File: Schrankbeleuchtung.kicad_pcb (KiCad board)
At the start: 2 copper layers, 77 x 60 mm, 27 parts, among them J1 Jack-DC, J2 Conn_01x02, J3 Conn_01x02, J4 Conn_01x02, J5 Conn_01x02, J6 Conn_01x02, J7 Conn_01x02, J8 Conn_01x02, J9 Conn_01x02, Q1 AO3400A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

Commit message: Edit description
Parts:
- moved J6 92.6 mm to (56.8, 71.0)
- moved J7 92.2 mm to (66.2, 71.0)
- moved J9 92.0 mm to (85.8, 71.0)
- moved J8 91.8 mm to (76.2, 71.0)
- moved Q4 75.6 mm to (63.4, 55.5), turned to 180 degrees
- moved Q3 75.0 mm to (59.5, 55.5), turned to 180 degrees
- moved Q2 74.2 mm to (55.5, 55.5), turned to 180 degrees
- moved Q1 73.5 mm to (51.6, 55.5), turned to 180 degrees
- moved R1 68.1 mm to (53.0, 60.5), turned to 90 degrees
- moved R2 68.1 mm to (56.5, 60.5), turned to 90 degrees
- moved R3 68.1 mm to (60.0, 60.5), turned to 90 degrees
- moved R4 68.1 mm to (63.5, 60.5), turned to 90 degrees
- moved R5 68.1 mm to (67.0, 60.5), turned to 90 degrees
- moved R6 68.1 mm to (70.5, 60.5), turned to 90 degrees
- moved R7 68.1 mm to (74.0, 60.5), turned to 90 degrees
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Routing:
- net +12V: track 29.7 -> 147.1 mm
- net +3.3V: track 75.3 -> 32.8 mm
- net Net-(J4-Pin_2): track 14.1 -> 50.4 mm
- net /GPIO09: track 54.2 -> 21.0 mm
- net /GPIO08: track 46.2 -> 13.4 mm
- net Net-(J5-Pin_2): track 19.3 -> 50.4 mm
- net Net-(J3-Pin_2): track 9.89 -> 40.0 mm
- net /GPIO07: track 41.1 -> 11.6 mm
- net Net-(J2-Pin_2): track 5.98 -> 30.0 mm
- net /GPIO06: track 34.5 -> 19.5 mm
- net /GPIO02: track 0.00 -> 4.05 mm
- net /GPIO05: track 5.90 -> 3.61 mm
- net /GPIO04: track 4.92 -> 3.21 mm
- net /GPIO03: track 4.65 -> 3.36 mm
- net GND: track 15.9 -> 14.8 mm
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- added copper zone on B.Cu, net GND
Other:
- board size 77 x 60 mm -> 55 x 60 mm

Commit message: Edit PCB layout
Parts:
- added H1: MountingHole_Pad, MountingHole:MountingHole_2.2mm_M2_ISO7380_Pad, F.Cu at (49.0, 83.0)
- added H2: MountingHole_Pad, MountingHole:MountingHole_2.2mm_M2_ISO7380_Pad, F.Cu at (96.0, 83.0)
- added H3: MountingHole_Pad, MountingHole:MountingHole_2.2mm_M2_ISO7380_Pad, F.Cu at (96.0, 31.0)
- A1: value RaspberryPi_Pico -> SC0918
- C1: value 220µF -> 100µF; footprint Capacitor_SMD:C_1206_3216Metric -> Capacitor_SMD:CP_Elec_6.3x5.8
- C2: value 220µF -> 100µF; footprint Capacitor_SMD:C_1206_3216Metric -> Capacitor_SMD:C_1210_3225Metric
- J1: value Jack-DC -> 694106301002; footprint Connector_BarrelJack:BarrelJack_GCT_DCJ200-10-A_Horizontal -> Connector_BarrelJack:BarrelJack_Horizontal
- J2, J3, J4, J5, J6, J7, J8, J9: value Conn_01x02 -> B2B-XH-AMLFSNP
- L1: value DR127-330-R -> 33µH; footprint footprints:IND_DR127-330-R_EAT -> Inductor_SMD:L_7.3x7.3_H3.5
- Q1, Q2, Q3, Q4: value AO3400A -> IRLML6344
- moved D1 4.27 mm to (93.5, 40.0), turned to 0 degrees
- moved C2 3.61 mm to (81.0, 31.0), turned to 90 degrees
- moved L1 3.35 mm to (89.0, 32.5), turned to 180 degrees
- moved C1 3.00 mm to (81.0, 38.5)
- moved U1 1.22 mm to (65.3, 35.0)
- moved J1 1.20 mm to (55.5, 35.0), turned to 0 degrees
- moved Q3 0.08 mm to (59.4, 55.5)
- moved Q4 0.06 mm to (63.5, 55.5)
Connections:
- J1 pad 3: (no net) -> unconnected-(J1-Pad3)
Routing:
- net GND: track 14.8 -> 109.8 mm, vias 10 -> 26
- net +12V: track 147.1 -> 142.4 mm
- net Net-(U1-FB): track 18.4 -> 14.9 mm
- net +5V: track 52.1 -> 54.2 mm
- net (no net): vias 3 -> 0

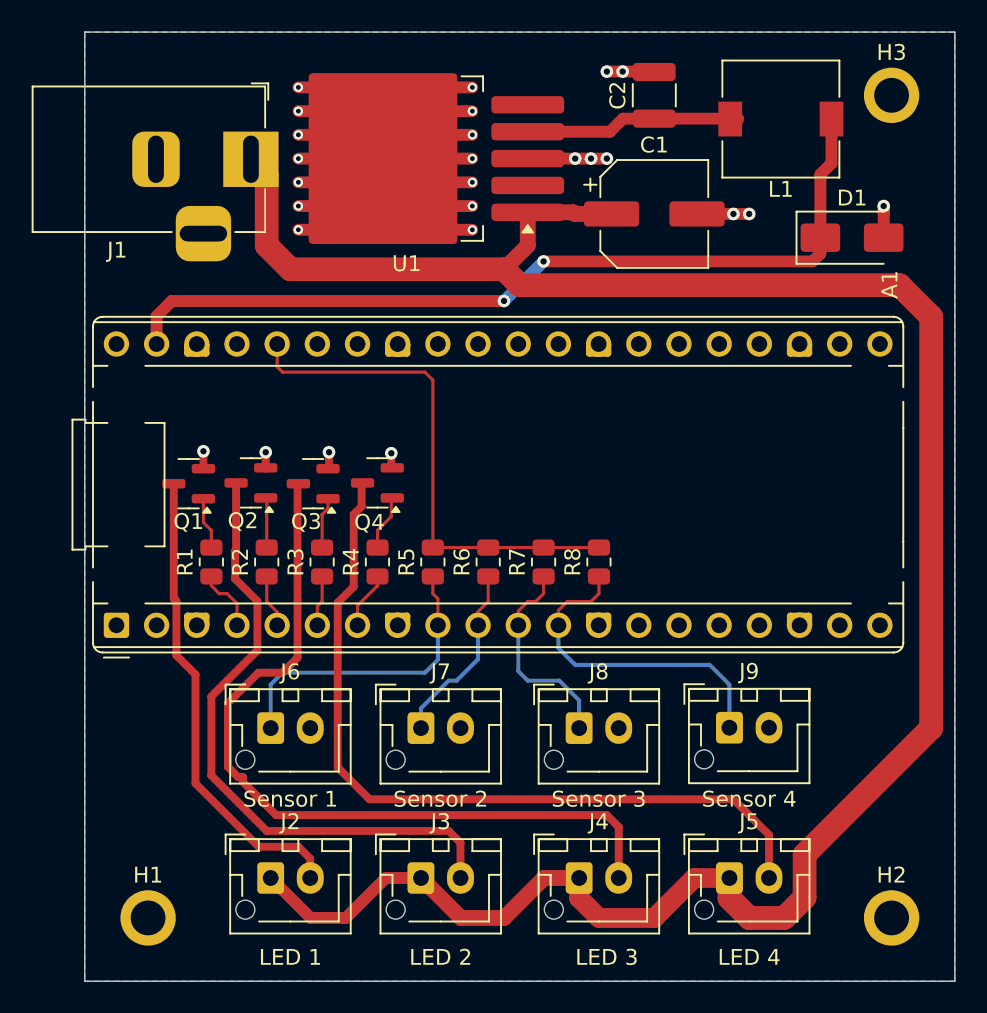
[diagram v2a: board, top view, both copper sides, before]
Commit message: Spannungswandler geändert. Stückliste aktualisiert.
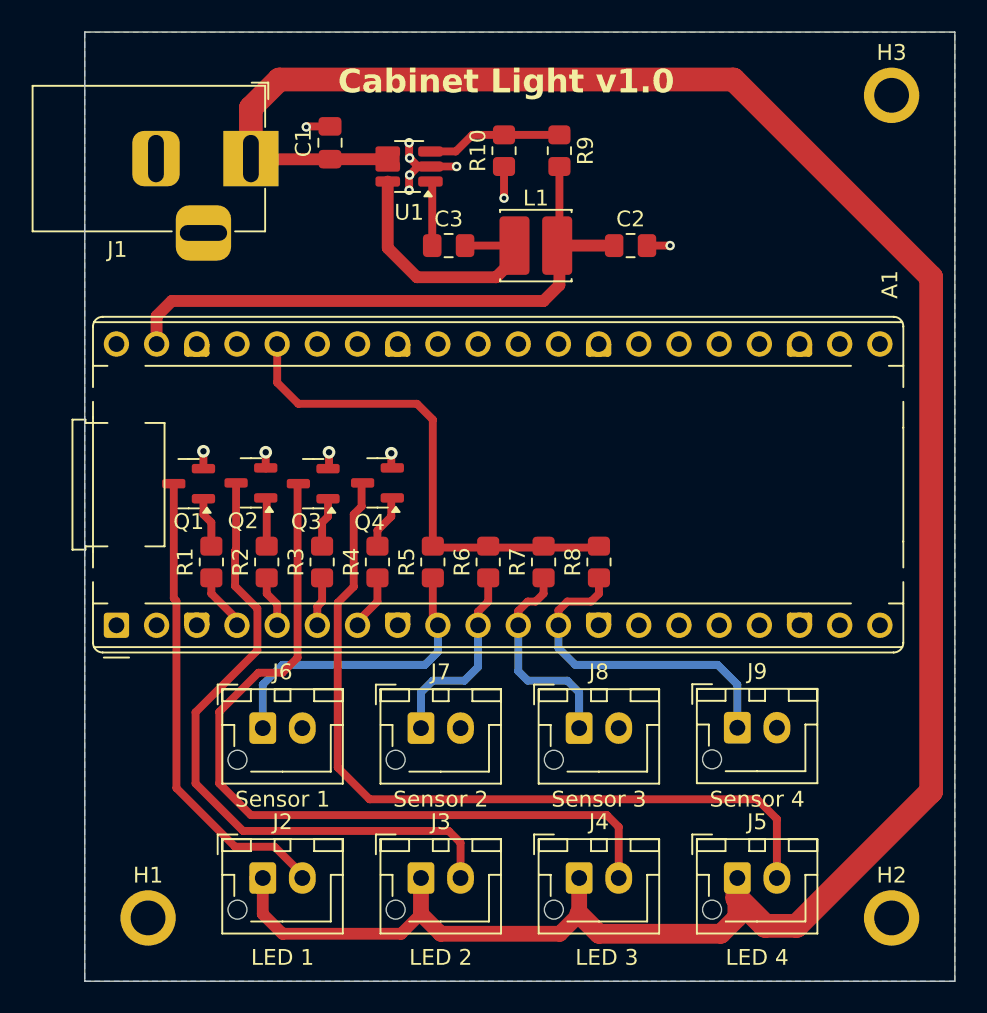
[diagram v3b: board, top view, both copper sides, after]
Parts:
- removed D1: SS34, Diode_SMD:D_SMA
- added C3: 0.1µF, Capacitor_SMD:C_0805_2012Metric_Pad1.18x1.45mm_HandSolder, F.Cu at (68.0, 40.5)
- added R10: 3.16k, Resistor_SMD:R_0805_2012Metric_Pad1.20x1.40mm_HandSolder, F.Cu at (71.5, 34.5)
- added R9: 10k, Resistor_SMD:R_0805_2012Metric_Pad1.20x1.40mm_HandSolder, F.Cu at (75.0, 34.5)
- C1: value 100µF -> 10µF; footprint Capacitor_SMD:CP_Elec_6.3x5.8 -> Capacitor_SMD:C_0805_2012Metric_Pad1.18x1.45mm_HandSolder
- C2: value 100µF -> 22µF; footprint Capacitor_SMD:C_1210_3225Metric -> Capacitor_SMD:C_0805_2012Metric_Pad1.18x1.45mm_HandSolder
- L1: value 33µH -> 10µH; footprint Inductor_SMD:L_7.3x7.3_H3.5 -> Inductor_SMD:L_Cenker_CKCS4030
- R1, R2, R3, R4, R5, R6, R7, R8: footprint Resistor_SMD:R_0805_2012Metric -> Resistor_SMD:R_0805_2012Metric_Pad1.20x1.40mm_HandSolder
- U1: value LM2596S-5 -> TPS560430XDBVT; footprint Package_TO_SOT_SMD:TO-263-5_TabPin3 -> Package_TO_SOT_SMD:SOT-23-6_Handsoldering
- moved C1 21.0 mm to (60.5, 34.0), turned to 90 degrees
- moved L1 17.4 mm to (73.5, 40.5), turned to 0 degrees
- moved C2 9.62 mm to (79.5, 40.5), turned to 0 degrees
- moved U1 0.52 mm to (65.5, 35.5)
- moved J2 0.50 mm to (56.2, 80.5)
- moved J5 0.50 mm to (86.2, 80.5)
- moved J6 0.50 mm to (56.2, 71.0)
- moved J9 0.50 mm to (86.2, 71.0)
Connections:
- C2 pad 1: Net-(U1-FB) -> +5V
- L1 pad 1: +5V -> Net-(U1-SW)
- L1 pad 2: Net-(U1-FB) -> +5V
- U1 pad 1: +12V -> Net-(U1-CB)
- U1 pad 2: unconnected-(U1-OUT-Pad2) -> GND
- U1 pad 3: GND -> Net-(U1-FB)
- U1 pad 4: Net-(U1-FB) -> +12V
- U1 pad 5: unconnected-(U1-~{ON}/OFF-Pad5) -> +12V
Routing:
- net GND: track 109.8 -> 14.9 mm, vias 26 -> 12
- net Net-(U1-SW): track 0.00 -> 17.2 mm
- net +5V: track 54.2 -> 39.0 mm, vias 2 -> 0
- net +12V: track 142.4 -> 155.7 mm
- net Net-(U1-FB): track 14.9 -> 8.58 mm
- net Net-(U1-CB): track 0.00 -> 4.10 mm
- net Net-(J3-Pin_2): track 40.0 -> 41.7 mm
- net Net-(J5-Pin_2): track 50.4 -> 51.7 mm
- net Net-(J4-Pin_2): track 50.4 -> 51.6 mm
- net /GPIO07: track 11.6 -> 12.5 mm
- net +3.3V: track 32.8 -> 31.9 mm
- net /GPIO09: track 21.0 -> 21.8 mm
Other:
- board text added: "Cabinet Light v1.0"

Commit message: PCB Layoutupdate
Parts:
- added H4: MountingHole_Pad, MountingHole:MountingHole_2.2mm_M2_ISO7380_Pad, F.Cu at (48.0, 48.0)
- J2, J3, J4, J5, J6, J7, J8, J9: footprint Connector_JST:JST_XH_B2B-XH-AM_1x02_P2.50mm_Vertical -> Connector_JST:JST_XH_B2B-XH-A_1x02_P2.50mm_Vertical
- Q1, Q2, Q3, Q4: value IRLML6344 -> IRLML0030TRPBF
- R1, R2, R3, R4: value 100R -> 187R
- moved J1 43.0 mm to (55.0, 78.0)
- moved C1 33.0 mm to (79.5, 61.0), turned to 0 degrees
- moved R10 31.6 mm to (68.5, 66.0), turned to 180 degrees
- moved C2 29.3 mm to (54.0, 55.0), turned to 180 degrees
- moved R9 28.7 mm to (68.5, 62.5), turned to 180 degrees
- moved U1 26.6 mm to (74.5, 60.5), turned to 0 degrees
- moved L1 17.6 mm to (69.0, 57.5), turned to 180 degrees
- moved H3 17.0 mm to (97.0, 48.0)
- moved C3 16.6 mm to (74.0, 56.0)
- moved R6 10.1 mm to (79.5, 65.0)
- moved R5 10.1 mm to (75.4, 66.0), turned to 0 degrees
- moved R7 9.23 mm to (82.1, 65.0)
- moved R8 8.41 mm to (84.6, 65.0)
- moved J6 8.19 mm to (60.5, 78.0)
- moved J7 7.94 mm to (70.0, 78.0)
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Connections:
- A1 pad 10: /GPIO07 -> unconnected-(A1-GPIO7-Pad10)
- A1 pad 11: /GPIO08 -> unconnected-(A1-GPIO8-Pad11)
- A1 pad 12: /GPIO09 -> /GPIO06
- A1 pad 14: unconnected-(A1-GPIO10-Pad14) -> /GPIO07
- A1 pad 15: unconnected-(A1-GPIO11-Pad15) -> /GPIO08
- A1 pad 16: unconnected-(A1-GPIO12-Pad16) -> /GPIO09
- A1 pad 9: /GPIO06 -> unconnected-(A1-GPIO6-Pad9)
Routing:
- net +12V: track 155.7 -> 134.7 mm, vias 0 -> 2
- net +3.3V: track 31.9 -> 51.7 mm
- net +5V: track 39.0 -> 26.0 mm
- net /GPIO09: track 21.8 -> 14.0 mm
- net /GPIO07: track 12.5 -> 20.2 mm
- net Net-(J4-Pin_2): track 51.6 -> 44.1 mm
- net Net-(U1-SW): track 17.2 -> 12.3 mm
- net Net-(J3-Pin_2): track 41.7 -> 37.4 mm
- net /GPIO06: track 19.9 -> 24.0 mm
- net Net-(Q2-G): track 3.11 -> 5.61 mm
- net /GPIO03: track 3.36 -> 4.98 mm
- net /GPIO04: track 3.21 -> 4.59 mm
- net /GPIO05: track 3.61 -> 4.94 mm
- net /GPIO02: track 3.76 -> 4.77 mm
- net Net-(J2-Pin_2): track 30.3 -> 31.2 mm
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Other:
- board size 55 x 60 mm -> 55 x 45 mm
